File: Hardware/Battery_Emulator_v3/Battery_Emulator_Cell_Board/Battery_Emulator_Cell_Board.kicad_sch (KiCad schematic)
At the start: 32 parts, among them J3 Cell1_Vout, J4 Conn_01x05, Q1 IRFB7545PBF, U1 LM317_TO-220, U2 ISO1640BDR, U3 MCP4651T-103E_ST, U4 KA78M05_TO252, U5 MCP6001UT-I/OT

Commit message: Updated mother board + cell PCB
Made +12V trace on mother board 2mm so it can withstand 2A. Improved routing a bit. Changed pinheader to pinsocket on motherboard and pinsocket to pinheader on cell PCB. Mother board is nearly finished, Cell PCB is not finished.
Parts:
- J4: footprint Connector_PinSocket_2.54mm:PinSocket_1x05_P2.54mm_Horizontal -> Connector_PinHeader_2.54mm:PinHeader_1x05_P2.54mm_Horizontal
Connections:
- net +5V: now also J4.3 (Pin_3); no longer J4.2 (Pin_2)
- net GND: now also C3.2, J4.2 (Pin_2), PS1.1 (-Vin); no longer J4.5 (Pin_5)
- net SCL: now also J4.5 (Pin_5); no longer J4.4 (Pin_4)
- net SDA: now also J4.4 (Pin_4); no longer J4.3 (Pin_3)

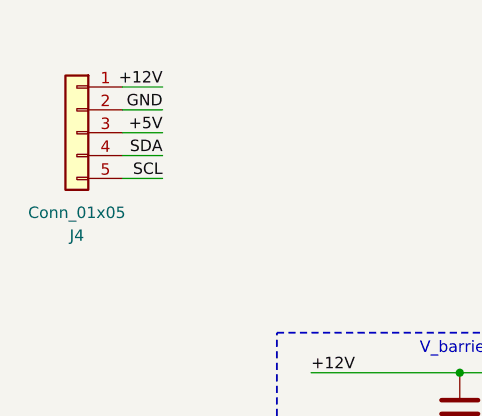
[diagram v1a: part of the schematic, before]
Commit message: Updated Mother board and Cell board
Changed pinout of mother board and cell board such that the pin headers are on the top side. Finished mother board PCB and did DRC check on it.
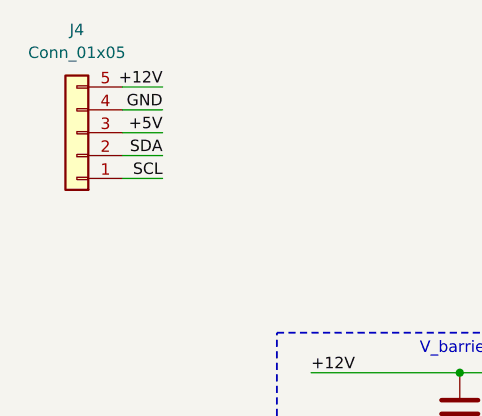
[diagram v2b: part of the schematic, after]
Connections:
- net +12V: now also J4.5 (Pin_5); no longer J4.1 (Pin_1)
- net GND: now also J4.4 (Pin_4); no longer J4.2 (Pin_2)
- net SCL: now also J4.1 (Pin_1); no longer J4.5 (Pin_5)
- net SDA: now also J4.2 (Pin_2); no longer J4.4 (Pin_4)
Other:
- moved on the sheet: J4
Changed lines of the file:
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@@
     )
   )
-  (symbol (lib_id "Connector_Generic:Conn_01x05") (at 22.86 31.115 0) (mirror y) (unit 1)
+  (symbol (lib_id "Connector_Generic:Conn_01x05") (at 22.86 31.115 180) (unit 1)
     (in_bom yes) (on_board yes) (dnp no)
-    (property "Reference" "J4" (at 22.86 42.545 0)
+    (property "Reference" "J4" (at 22.86 19.685 0)
       (effects (font (size 1.27 1.27)))
     )
-    (property "Value" "Conn_01x05" (at 22.86 40.005 0)
+    (property "Value" "Conn_01x05" (at 22.86 22.225 0)
       (effects (font (size 1.27 1.27)))
     )

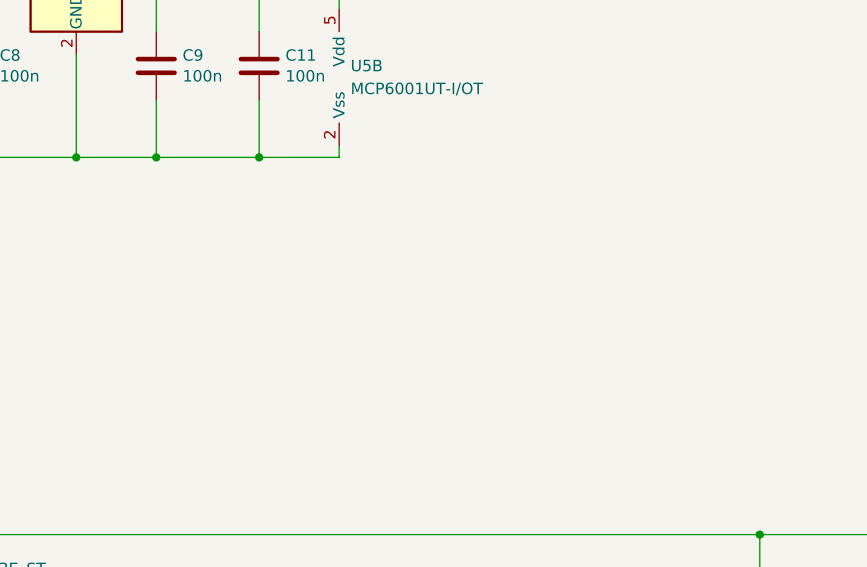
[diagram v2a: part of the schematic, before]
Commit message: Hardware Update
Added the symbols for the LT3080, and the transistor
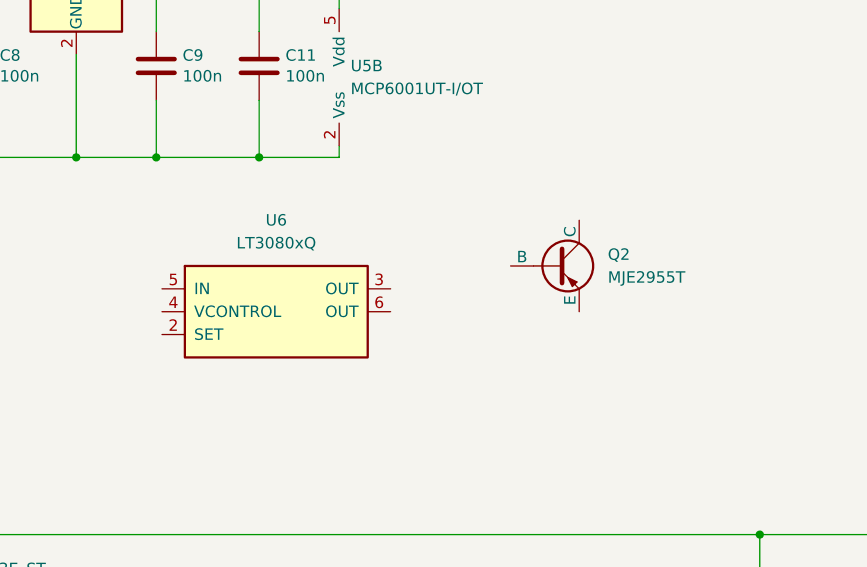
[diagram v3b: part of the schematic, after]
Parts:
- added Q2: MJE2955T, Package_TO_SOT_THT:TO-220-3_Horizontal_TabUp, symbol Simulation_SPICE:PNP
- added U6: LT3080xQ, Package_TO_SOT_SMD:TO-263-5_TabPin3, symbol Regulator_Linear:LT3080xQ
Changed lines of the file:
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@@
+    )
+  )
+  (symbol (lib_id "Simulation_SPICE:PNP") (at 186.055 85.09 0) (unit 1)
+    (in_bom yes) (on_board yes) (dnp no) (fields_autoplaced)
+    (property "Reference" "Q2" (at 191.77 83.82 0)
+      (effects (font (size 1.27 1.27)) (justify left))
+    )
+    (property "Value" "MJE2955T" (at 191.77 86.36 0)
+      (effects (font (size 1.27 1.27)) (justify left))
+    )
+    (property "Footprint" "Package_TO_SOT_THT:TO-220-3_Horizontal_TabUp" (at 221.615 85.09 0)
+      (effects (font (size 1.27 1.27)) hide)
+    )
+    (property "Datasheet" "https://nl.mouser.com/ProductDetail/STMicroelectronics/MJE2955T?qs=JV7lzlMm3yImIykVLh8MEA%3D%3D&mgh=1&gad_source=1&gclid=Cj0KCQiA35urBhDCARIsAOU7Qwkfu-vUx2w2rsEmrBOL6k7UZrNgrutFokRdKCIOhPiDj3gvUHFVAycaAkebEALw_wcB" (at 221.615 85.09 0)
+      (effects (font (size 1.27 1.27)) hide)
+    )
+    (property "Sim.Device" "PNP" (at 186.055 85.09 0)
+      (effects (font (size 1.27 1.27)) hide)
+    )
+    (property "Sim.Type" "GUMMELPOON" (at 186.055 85.09 0)
+      (effects (font (size 1.27 1.27)) hide)
+    )
+    (property "Sim.Pins" "1=B 2=C 3=E" (at 186.055 85.09 0)
+      (effects (font (size 1.27 1.27)) hide)
+    )
+    (pin "1")
+    (pin "2")
+    (pin "3")
+    (instances
+      (project "Battery_Emulator_Cell_Board"
+        (path "/180aea6f-6c78-4f59-bff6-104a9c25165d"
+          (reference "Q2") (unit 1)
+        )
+      )
     )
   )
@@
         )
       )
+    )
+  )
+  (symbol (lib_id "Regulator_Linear:LT3080xQ") (at 154.94 90.17 0) (unit 1)
+    (in_bom yes) (on_board yes) (dnp no) (fields_autoplaced)
+    (property "Reference" "U6" (at 154.94 80.01 0)
+      (effects (font (size 1.27 1.27)))
+    )
+    (property "Value" "LT3080xQ" (at 154.94 82.55 0)
+      (effects (font (size 1.27 1.27)))
+    )
+    (property "Footprint" "Package_TO_SOT_SMD:TO-263-5_TabPin3" (at 154.94 97.79 0)
+      (effects (font (size 1.27 1.27)) hide)
+    )
+    (property "Datasheet" "https://www.analog.com/media/en/technical-documentation/data-sheets/3080fc.pdf" (at 111.252 70.612 0)
+      (effects (font (size 1.27 1.27)) hide)
+    )
+    (pin "1")
+    (pin "2")
+    (pin "3")
+    (pin "4")
+    (pin "5")
+    (pin "6")
+    (instances
+      (project "Battery_Emulator_Cell_Board"
+        (path "/180aea6f-6c78-4f59-bff6-104a9c25165d"
+          (reference "U6") (unit 1)
+        )
+      )

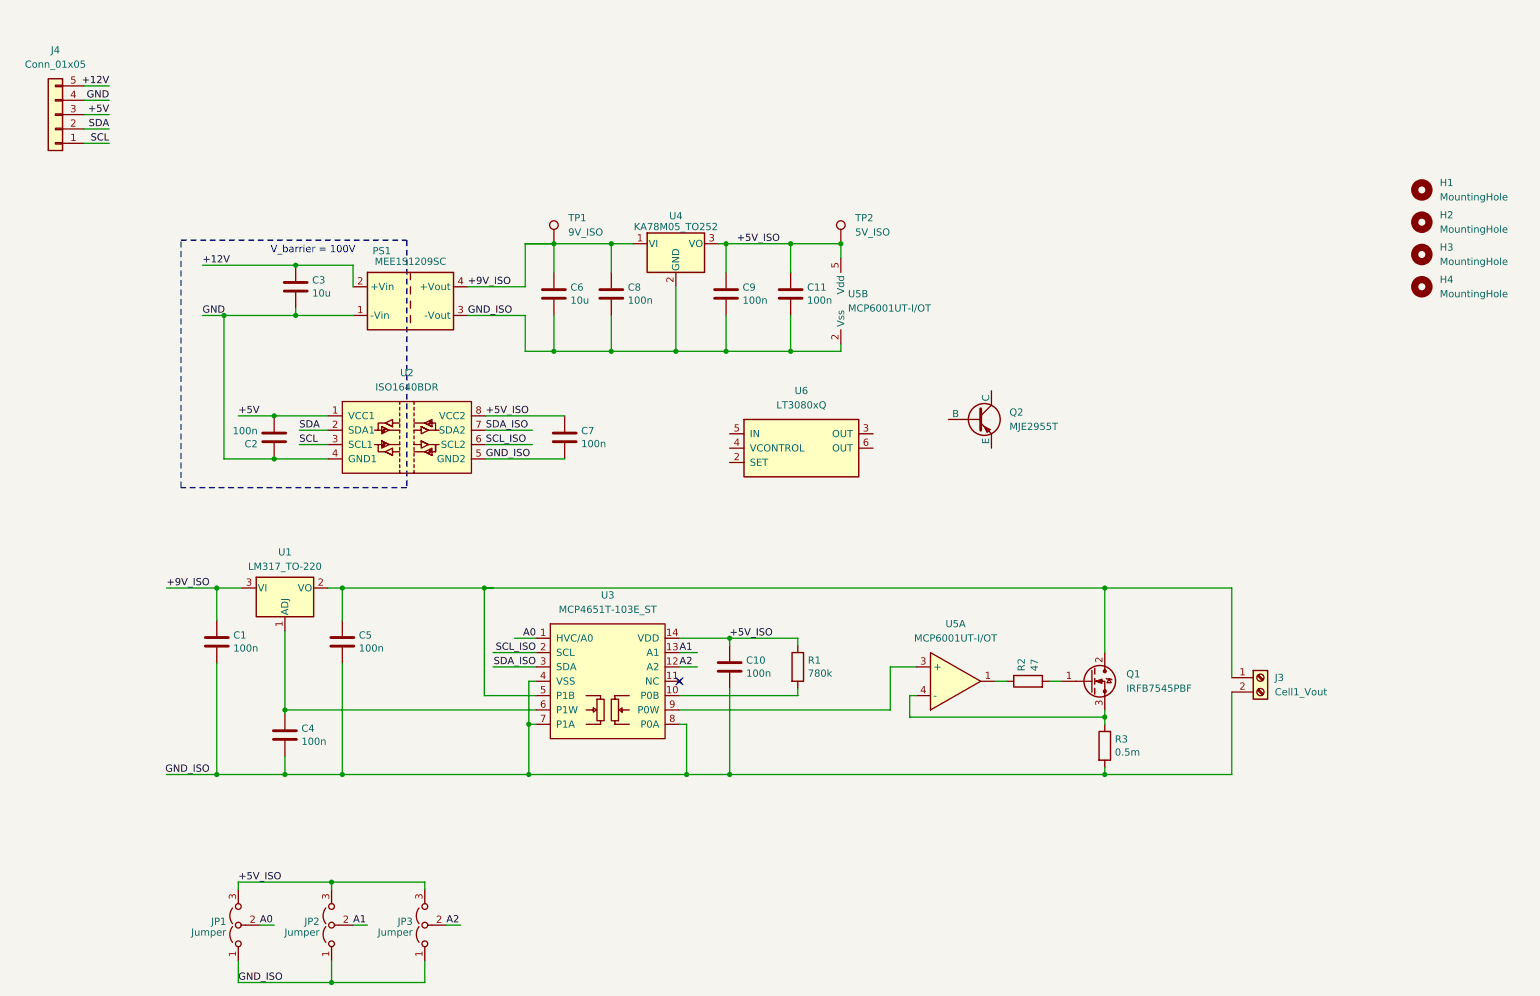
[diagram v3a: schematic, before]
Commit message: Update Battery_Emulator_Cell_Board.kicad_sch
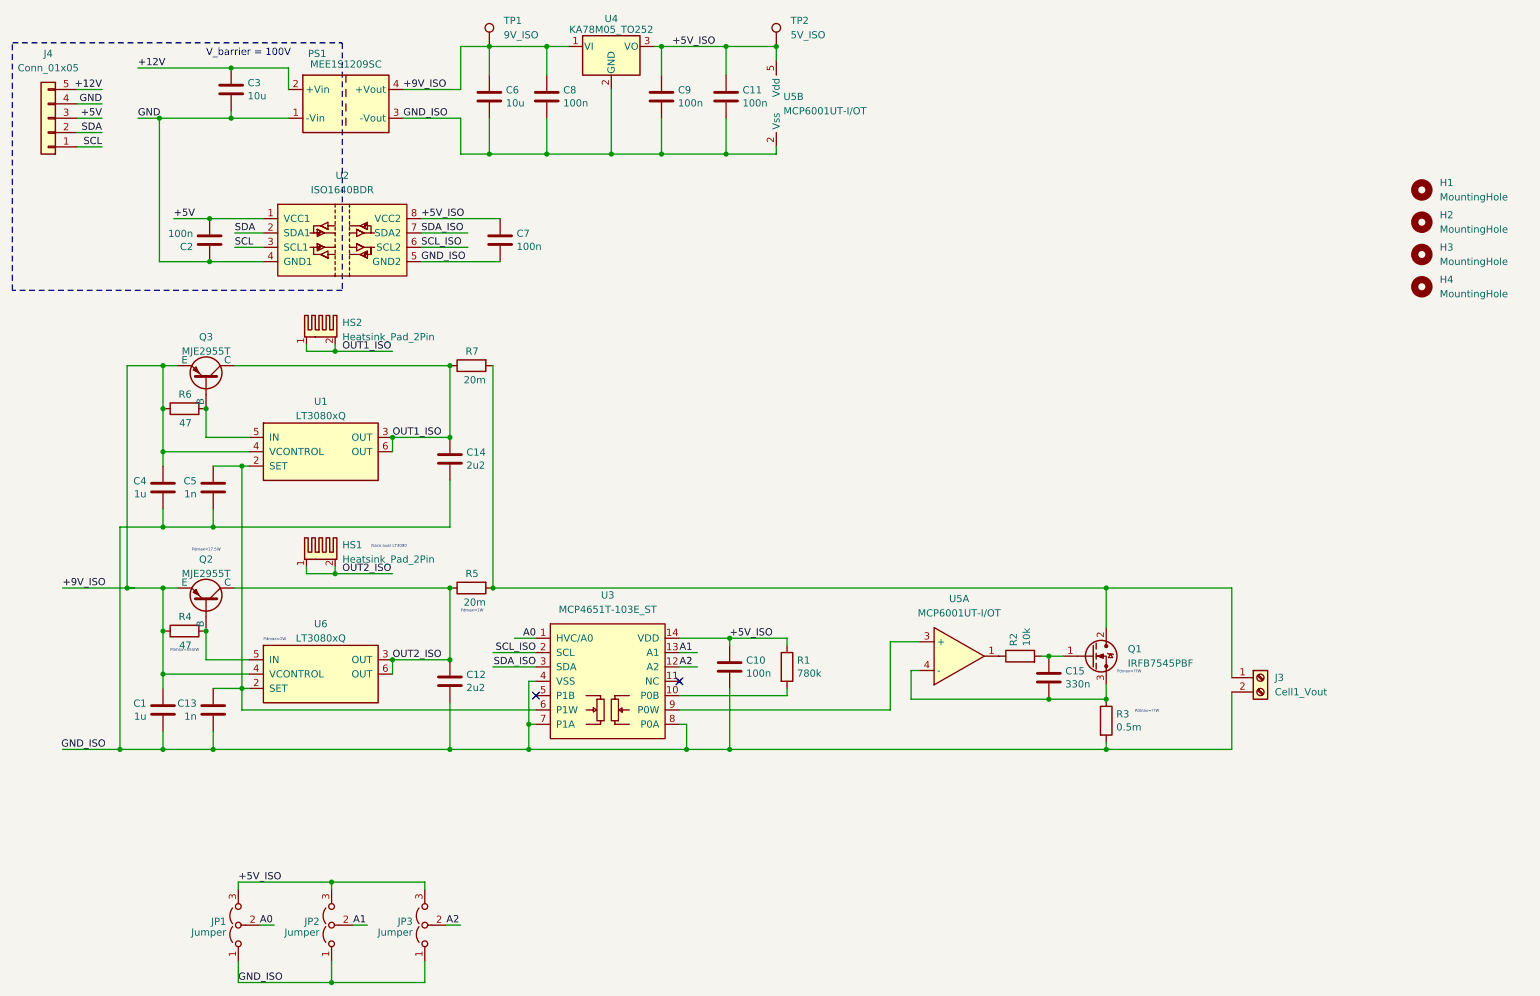
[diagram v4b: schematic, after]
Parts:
- removed U1: LM317_TO-220, Package_TO_SOT_THT:TO-220-3_Horizontal_TabUp, symbol Regulator_Linear:LM317_TO-220
- added C12, C14: 2u2, Capacitor_SMD:C_0805_2012Metric, symbol Device:C
- added C13: 1n, Capacitor_SMD:C_0805_2012Metric, symbol Device:C
- added C15: 330n, Capacitor_SMD:C_0805_2012Metric, symbol Device:C
- added HS1, HS2: Heatsink_Pad_2Pin, Heatsink:Heatsink_AAVID_573300D00010G_TO-263, symbol Mechanical:Heatsink_Pad_2Pin
- added Q3: MJE2955T, Package_TO_SOT_THT:TO-220-3_Horizontal_TabUp, symbol Simulation_SPICE:PNP
- added R4, R6: 47, Resistor_SMD:R_0805_2012Metric, symbol Device:R
- added R5, R7: 20m, Resistor_SMD:R_2512_6332Metric, symbol Device:R
- added U1: LT3080xQ, Package_TO_SOT_SMD:TO-263-5_TabPin3, symbol Regulator_Linear:LT3080xQ
- C1, C4: value 100n -> 1u
- C5: value 100n -> 1n
- R2: value 47 -> 10k
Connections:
- net +9V_ISO: now also C4.1, Q2.3 (E), U6.4 (VCONTROL), Q3.3 (E), R4.1, R6.1, U1.4 (VCONTROL)
- net GND_ISO: now also C12.2, C13.2, C14.2
- net at Q1.3, R3.1, U5.4 (-): now also C15.2
- net at U3.6 (P1W): now also C5.1, U6.2 (SET), C13.1, U1.2 (SET); no longer C4.1
- net at J3.1 (Pin_1), Q1.2, Q1.7 (D): now also R5.2, R7.2; no longer C5.1, U3.5 (P1B)
- net at Q1.1, R2.2: now also C15.1
- net OUT2_ISO: now reaches Q2.1 (C)
- net OUT2_ISO: now also U6.3 (OUT), U6.6 (OUT), C12.1, HS1.1, HS1.2, R5.1
- net at Q2.2 (B): now also U6.5 (IN), R4.2
- new net: Q3.2 (B), R6.2, U1.5 (IN)
- new net OUT1_ISO: C14.1, HS2.1, HS2.2, Q3.1 (C), R7.1, U1.3 (OUT), U1.6 (OUT)
- no-connect marks 1 -> 2
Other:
- note added: "Pdmax=17.5W"
- note added: "Pdmax=1W"
- note added: "Pdmax=2W"
- note added: "Pdmax=55mW"
- note added: "Pdmax=??W"
- note added: "Place over LT3080"
- moved on the sheet: C11, C2, C3, C6, C7, C8, C9, J4, PS1, Q1, Q2, R1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
